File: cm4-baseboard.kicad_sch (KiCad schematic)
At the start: 4 parts

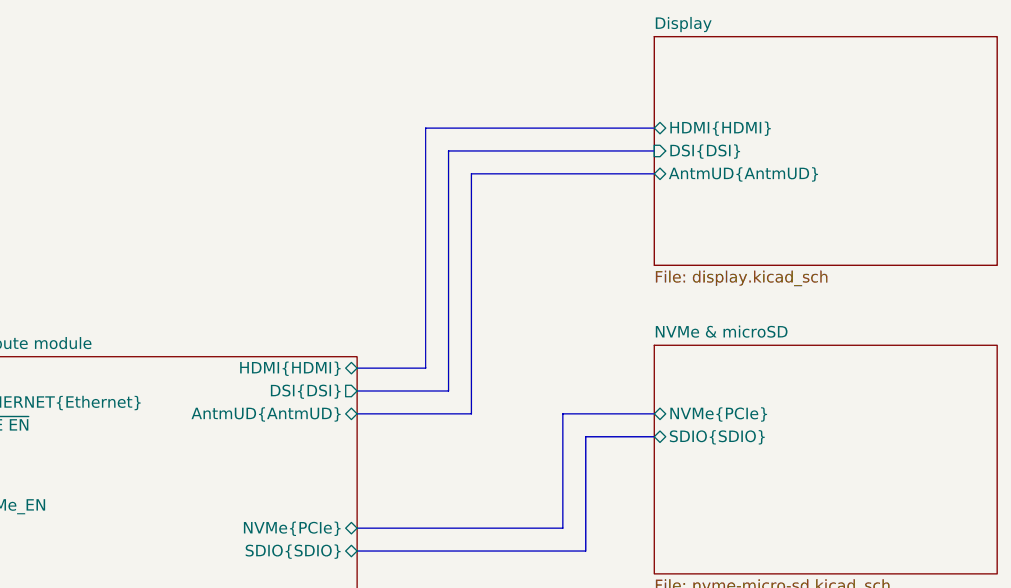
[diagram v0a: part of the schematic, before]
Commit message: [#54617] Update bus naming; remove DNP for TVS
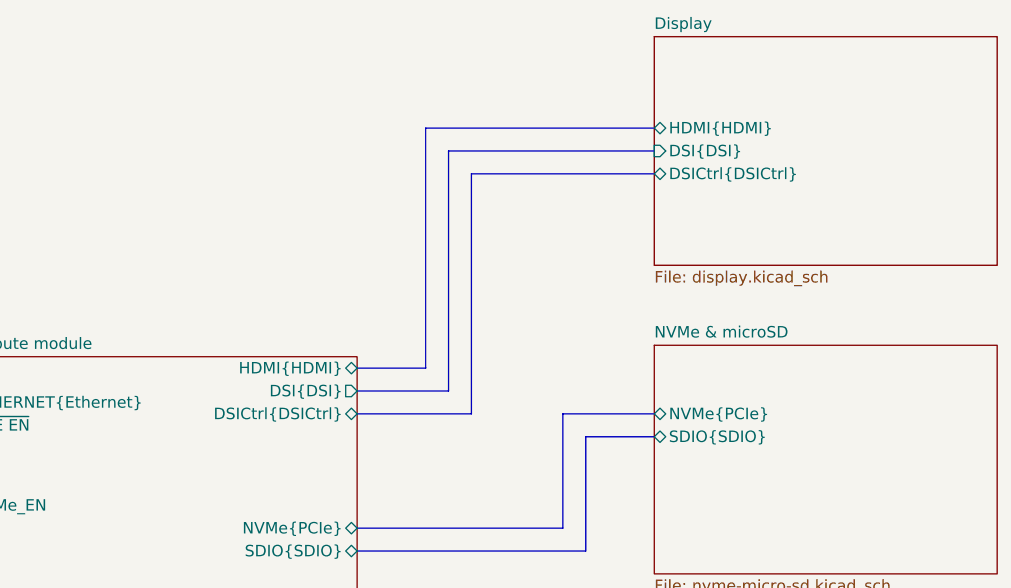
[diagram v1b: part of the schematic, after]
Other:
- sheet Compute module ports: added DSICtrl{DSICtrl}; removed AntmUD{AntmUD}
- sheet Display ports: added DSICtrl{DSICtrl}; removed AntmUD{AntmUD}
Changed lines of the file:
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@@
       (effects (font (size 1.27 1.27)) (justify right))
     )
-    (pin "AntmUD{AntmUD}" bidirectional (at 243.84 107.95 0)
+    (pin "DSICtrl{DSICtrl}" bidirectional (at 243.84 107.95 0)
       (effects (font (size 1.27 1.27)) (justify right))
     )
@@
       (effects (font (size 1.27 1.27)) (justify left))
     )
-    (pin "AntmUD{AntmUD}" bidirectional (at 276.86 81.28 180)
-      (effects (font (size 1.27 1.27)) (justify left))
-    )
+    (pin "DSICtrl{DSICtrl}" bidirectional (at 276.86 81.28 180)
+      (effects (font (size 1.27 1.27)) (justify left))
+    )

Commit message: [#54617] Review requested changes
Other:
- sheet Peripherials ports: added GPIO{GPIO}; removed none
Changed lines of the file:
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@@
+    (stroke (width 0) (type default))
+  )
+  (bus (pts (xy 261.62 149.86) (xy 276.86 149.86))
+    (stroke (width 0) (type default))
+  )
+  (bus (pts (xy 261.62 139.7) (xy 261.62 149.86))
     (stroke (width 0) (type default))
   )
@@
   )
   (bus (pts (xy 191.77 106.68) (xy 199.39 106.68))
+    (stroke (width 0) (type default))
+  )
+  (bus (pts (xy 243.84 139.7) (xy 261.62 139.7))
     (stroke (width 0) (type default))
   )
@@
       (effects (font (size 1.27 1.27)) (justify left))
     )
+    (pin "GPIO{GPIO}" bidirectional (at 276.86 149.86 180)
+      (effects (font (size 1.27 1.27)) (justify left))
+    )

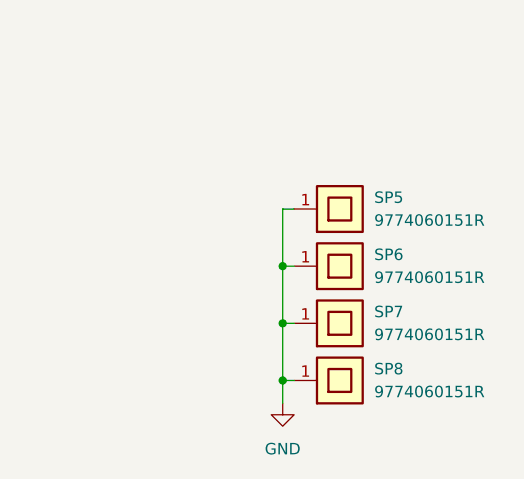
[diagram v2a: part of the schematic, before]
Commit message: [#54617] Re-enumerate reference designators
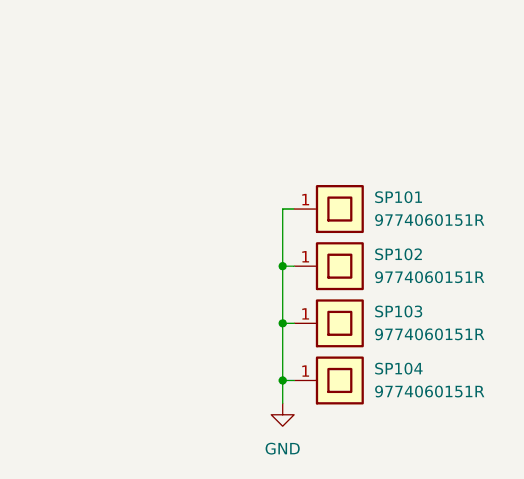
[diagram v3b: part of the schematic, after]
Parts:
- renumbered SP5 to SP101, SP6 to SP102, SP7 to SP103, SP8 to SP104
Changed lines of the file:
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@@
   (symbol (lib_id "antmicropower:GND") (at 379.73 240.03 0) (unit 1)
     (in_bom yes) (on_board yes) (dnp no) (fields_autoplaced)
-    (property "Reference" "#PWR0128" (at 388.62 242.57 0)
+    (property "Reference" "#PWR0101" (at 388.62 242.57 0)
       (effects (font (size 1.27 1.27) (thickness 0.15)) (justify left bottom) hide)
     )
@@
       (project "cm4-baseboard"
         (path "/60b842dc-0853-4a25-99ac-5784ddf94d0d"
-          (reference "#PWR0128") (unit 1)
+          (reference "#PWR0101") (unit 1)
         )
       )
@@
   (symbol (lib_id "antmicroMechanicalParts:Spacer_Drill3.7mm_H6mm_9774060151R") (at 381 224.79 0) (unit 1)
     (in_bom yes) (on_board yes) (dnp no)
-    (property "Reference" "SP6" (at 389.89 223.52 0)
+    (property "Reference" "SP102" (at 389.89 223.52 0)
       (effects (font (size 1.27 1.27)) (justify left))
     )
@@
       (project "cm4-baseboard"
         (path "/60b842dc-0853-4a25-99ac-5784ddf94d0d"
-          (reference "SP6") (unit 1)
+          (reference "SP102") (unit 1)
         )
       )
@@
   (symbol (lib_id "antmicroMechanicalParts:Spacer_Drill3.7mm_H6mm_9774060151R") (at 381 218.44 0) (unit 1)
     (in_bom yes) (on_board yes) (dnp no)
-    (property "Reference" "SP5" (at 389.89 217.17 0)
+    (property "Reference" "SP101" (at 389.89 217.17 0)
       (effects (font (size 1.27 1.27)) (justify left))
     )
@@
       (project "cm4-baseboard"
         (path "/60b842dc-0853-4a25-99ac-5784ddf94d0d"
-          (reference "SP5") (unit 1)
+          (reference "SP101") (unit 1)
         )
       )
@@
   (symbol (lib_id "antmicroMechanicalParts:Spacer_Drill3.7mm_H6mm_9774060151R") (at 381 237.49 0) (unit 1)
     (in_bom yes) (on_board yes) (dnp no)
-    (property "Reference" "SP8" (at 389.89 236.22 0)
+    (property "Reference" "SP104" (at 389.89 236.22 0)
       (effects (font (size 1.27 1.27)) (justify left))
     )
@@
       (project "cm4-baseboard"
         (path "/60b842dc-0853-4a25-99ac-5784ddf94d0d"
-          (reference "SP8") (unit 1)
+          (reference "SP104") (unit 1)
         )
       )
@@
   (symbol (lib_id "antmicroMechanicalParts:Spacer_Drill3.7mm_H6mm_9774060151R") (at 381 231.14 0) (unit 1)
     (in_bom yes) (on_board yes) (dnp no)
-    (property "Reference" "SP7" (at 389.89 229.87 0)
+    (property "Reference" "SP103" (at 389.89 229.87 0)
       (effects (font (size 1.27 1.27)) (justify left))
     )
@@
       (project "cm4-baseboard"
         (path "/60b842dc-0853-4a25-99ac-5784ddf94d0d"
-          (reference "SP7") (unit 1)
+          (reference "SP103") (unit 1)
         )
       )

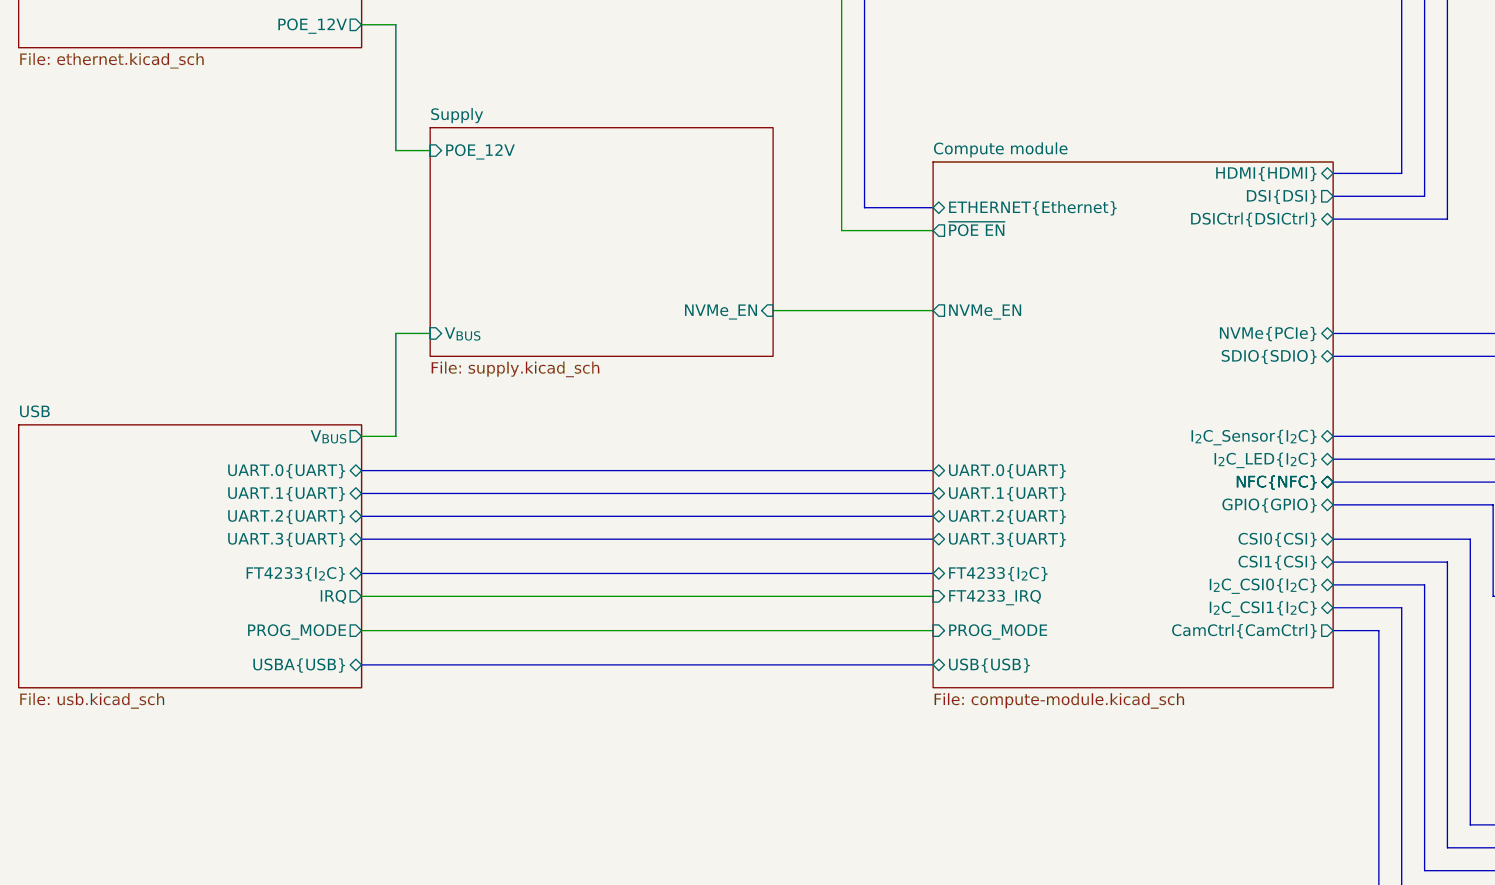
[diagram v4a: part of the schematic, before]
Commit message: [#55181] PCB: USB placement; Sch: minor USB related changes
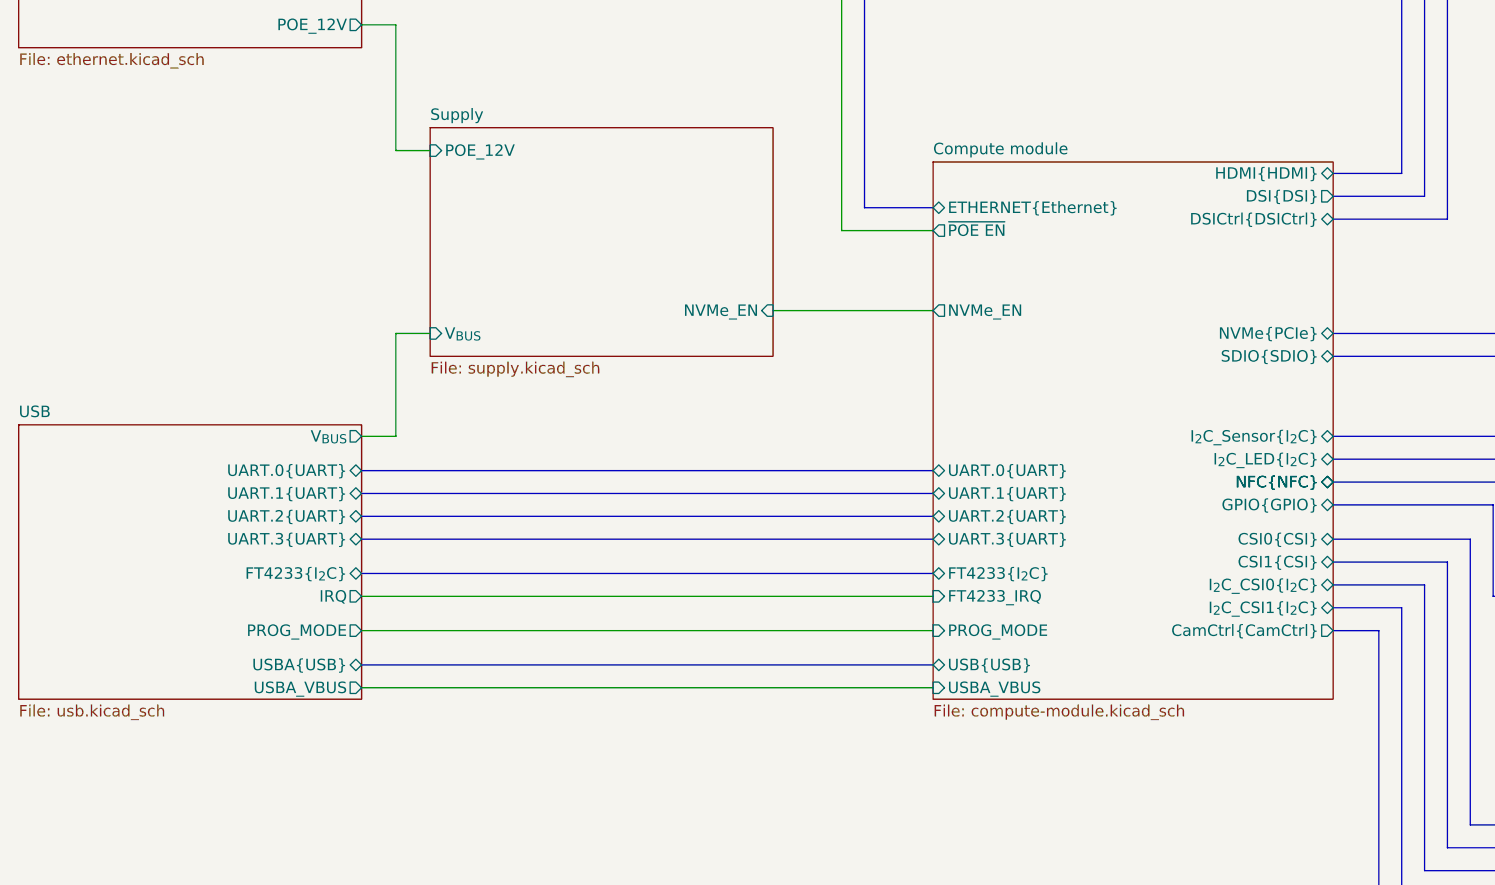
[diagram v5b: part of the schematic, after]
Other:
- sheet Compute module ports: added USBA_VBUS; removed none
- sheet USB ports: added USBA_VBUS; removed none
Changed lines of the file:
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@@
+    (stroke (width 0) (type default))
+  )
+  (wire (pts (xy 135.89 160.02) (xy 199.39 160.02))
     (stroke (width 0) (type default))
   )
@@
     )
   )
-  (sheet (at 199.39 101.6) (size 44.45 58.42) (fields_autoplaced)
+  (sheet (at 199.39 101.6) (size 44.45 59.69) (fields_autoplaced)
     (stroke (width 0) (type solid))
     (fill (color 0 0 0 0.0000))
@@
       (effects (font (size 1.27 1.27)) (justify left bottom))
     )
-    (property "Sheetfile" "compute-module.kicad_sch" (at 199.39 160.6046 0)
+    (property "Sheetfile" "compute-module.kicad_sch" (at 199.39 161.8746 0)
       (effects (font (size 1.27 1.27)) (justify left top))
     )
@@
     )
     (pin "FT4233{I_{2}C}" bidirectional (at 199.39 147.32 180)
+      (effects (font (size 1.27 1.27)) (justify left))
+    )
+    (pin "USBA_VBUS" input (at 199.39 160.02 180)
       (effects (font (size 1.27 1.27)) (justify left))
     )
@@
     )
   )
-  (sheet (at 97.79 130.81) (size 38.1 29.21) (fields_autoplaced)
+  (sheet (at 97.79 130.81) (size 38.1 30.48) (fields_autoplaced)
     (stroke (width 0.1524) (type solid))
     (fill (color 0 0 0 0.0000))
@@
       (effects (font (size 1.27 1.27)) (justify left bottom))
     )
-    (property "Sheetfile" "usb.kicad_sch" (at 97.79 160.6046 0)
+    (property "Sheetfile" "usb.kicad_sch" (at 97.79 161.8746 0)
       (effects (font (size 1.27 1.27)) (justify left top))
     )
@@
       (effects (font (size 1.27 1.27)) (justify right))
     )
+    (pin "USBA_VBUS" output (at 135.89 160.02 0)
+      (effects (font (size 1.27 1.27)) (justify right))
+    )

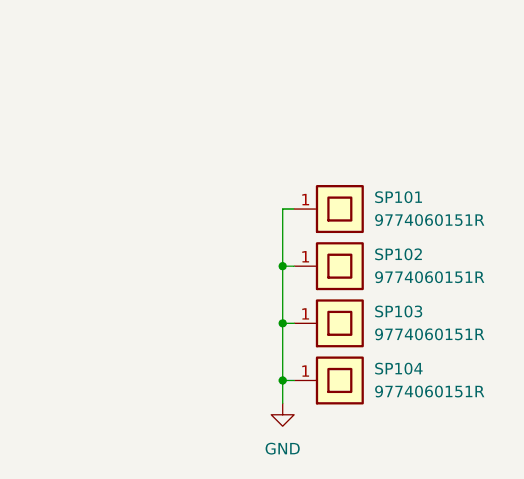
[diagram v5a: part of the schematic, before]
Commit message: [#55181] Change adapter spacer to 2mm; update spacers from lib
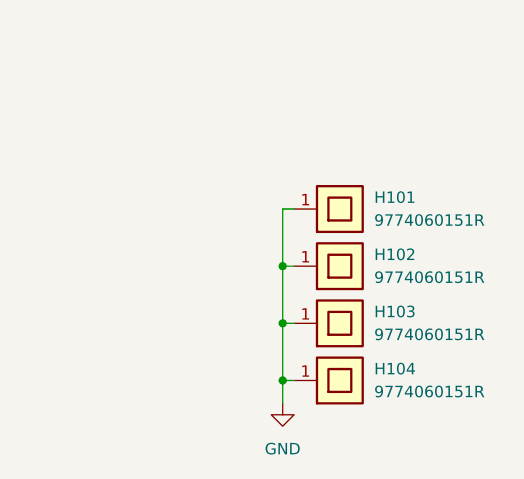
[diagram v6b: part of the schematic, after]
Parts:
- H101: renamed from SP101; value Spacer_H6mm_9774060151 -> Spacer_Drill3.7mm_H6mm_9774060151R
- H102: renamed from SP102; value Spacer_H6mm_9774060151 -> Spacer_Drill3.7mm_H6mm_9774060151R
- H103: renamed from SP103; value Spacer_H6mm_9774060151 -> Spacer_Drill3.7mm_H6mm_9774060151R
- H104: renamed from SP104; value Spacer_H6mm_9774060151 -> Spacer_Drill3.7mm_H6mm_9774060151R
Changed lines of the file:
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@@
   (symbol (lib_id "antmicroMechanicalParts:Spacer_Drill3.7mm_H6mm_9774060151R") (at 381 224.79 0) (unit 1)
     (in_bom yes) (on_board yes) (dnp no)
-    (property "Reference" "SP102" (at 389.89 223.52 0)
+    (property "Reference" "H102" (at 389.89 223.52 0)
       (effects (font (size 1.27 1.27)) (justify left))
     )
-    (property "Value" "Spacer_H6mm_9774060151" (at 389.89 224.7899 0)
+    (property "Value" "Spacer_Drill3.7mm_H6mm_9774060151R" (at 389.89 224.7899 0)
       (effects (font (size 1.27 1.27)) (justify left) hide)
     )
@@
       (project "cm4-baseboard"
         (path "/60b842dc-0853-4a25-99ac-5784ddf94d0d"
-          (reference "SP102") (unit 1)
+          (reference "H102") (unit 1)
         )
       )
@@
   (symbol (lib_id "antmicroMechanicalParts:Spacer_Drill3.7mm_H6mm_9774060151R") (at 381 218.44 0) (unit 1)
     (in_bom yes) (on_board yes) (dnp no)
-    (property "Reference" "SP101" (at 389.89 217.17 0)
+    (property "Reference" "H101" (at 389.89 217.17 0)
       (effects (font (size 1.27 1.27)) (justify left))
     )
-    (property "Value" "Spacer_H6mm_9774060151" (at 389.89 218.4399 0)
+    (property "Value" "Spacer_Drill3.7mm_H6mm_9774060151R" (at 389.89 218.4399 0)
       (effects (font (size 1.27 1.27)) (justify left) hide)
     )
@@
       (project "cm4-baseboard"
         (path "/60b842dc-0853-4a25-99ac-5784ddf94d0d"
-          (reference "SP101") (unit 1)
+          (reference "H101") (unit 1)
         )
       )
@@
   (symbol (lib_id "antmicroMechanicalParts:Spacer_Drill3.7mm_H6mm_9774060151R") (at 381 237.49 0) (unit 1)
     (in_bom yes) (on_board yes) (dnp no)
-    (property "Reference" "SP104" (at 389.89 236.22 0)
+    (property "Reference" "H104" (at 389.89 236.22 0)
       (effects (font (size 1.27 1.27)) (justify left))
     )
-    (property "Value" "Spacer_H6mm_9774060151" (at 389.89 237.4899 0)
+    (property "Value" "Spacer_Drill3.7mm_H6mm_9774060151R" (at 389.89 237.4899 0)
       (effects (font (size 1.27 1.27)) (justify left) hide)
     )
@@
       (project "cm4-baseboard"
         (path "/60b842dc-0853-4a25-99ac-5784ddf94d0d"
-          (reference "SP104") (unit 1)
+          (reference "H104") (unit 1)
         )
       )
@@
   (symbol (lib_id "antmicroMechanicalParts:Spacer_Drill3.7mm_H6mm_9774060151R") (at 381 231.14 0) (unit 1)
     (in_bom yes) (on_board yes) (dnp no)
-    (property "Reference" "SP103" (at 389.89 229.87 0)
+    (property "Reference" "H103" (at 389.89 229.87 0)
       (effects (font (size 1.27 1.27)) (justify left))
     )
-    (property "Value" "Spacer_H6mm_9774060151" (at 389.89 231.1399 0)
+    (property "Value" "Spacer_Drill3.7mm_H6mm_9774060151R" (at 389.89 231.1399 0)
       (effects (font (size 1.27 1.27)) (justify left) hide)
     )
@@
       (project "cm4-baseboard"
         (path "/60b842dc-0853-4a25-99ac-5784ddf94d0d"
-          (reference "SP103") (unit 1)
+          (reference "H103") (unit 1)
         )
       )

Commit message: [#55532] Sch: Optimize conections for easier routing
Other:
- sheet CSI ports: added I_{2}C1{I_{2}C}; removed I_{2}C_CSI1{I_{2}C}
- sheet Compute module ports: added I_{2}C1{I_{2}C}; removed FT4233{I_{2}C}, I_{2}C_CSI1{I_{2}C}, I_{2}C_LED{I_{2}C}, I_{2}C_Sensor{I_{2}C}
- sheet Display ports: added I_{2}C1{I_{2}C}; removed none
- sheet Peripherials ports: added I_{2}C1{I_{2}C}; removed I_{2}C_LED{I_{2}C}, I_{2}C_Sensor{I_{2}C}
- sheet USB ports: added I_{2}C1{I_{2}C}; removed FT4233{I_{2}C}
